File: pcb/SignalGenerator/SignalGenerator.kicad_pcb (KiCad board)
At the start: 2 copper layers, 29 parts, among them J1 ul.f antenna connector, U1 16 MHz, U2 MIC5205-3.3YM5, U3 AD9837, U4 AD8045

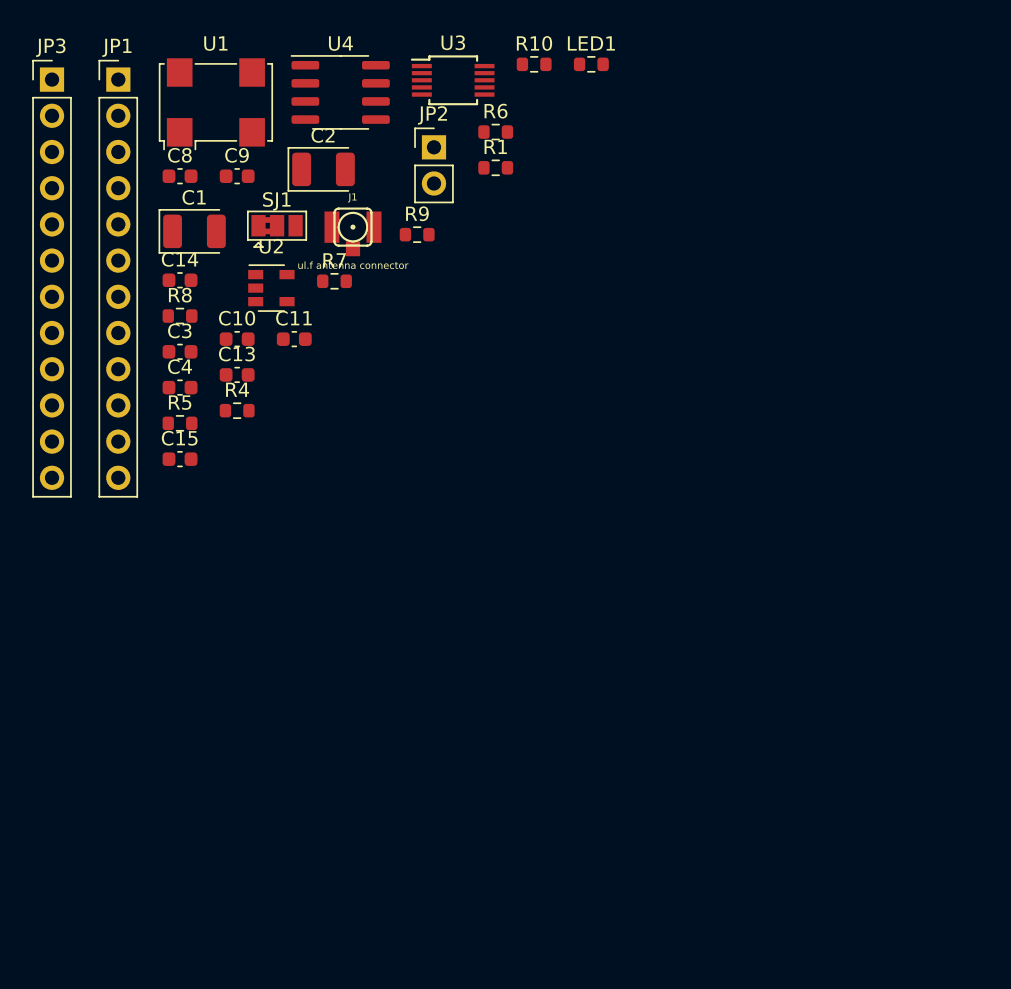
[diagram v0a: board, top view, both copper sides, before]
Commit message: Agrego modelo correcto para U3, y ubicación de los componentes
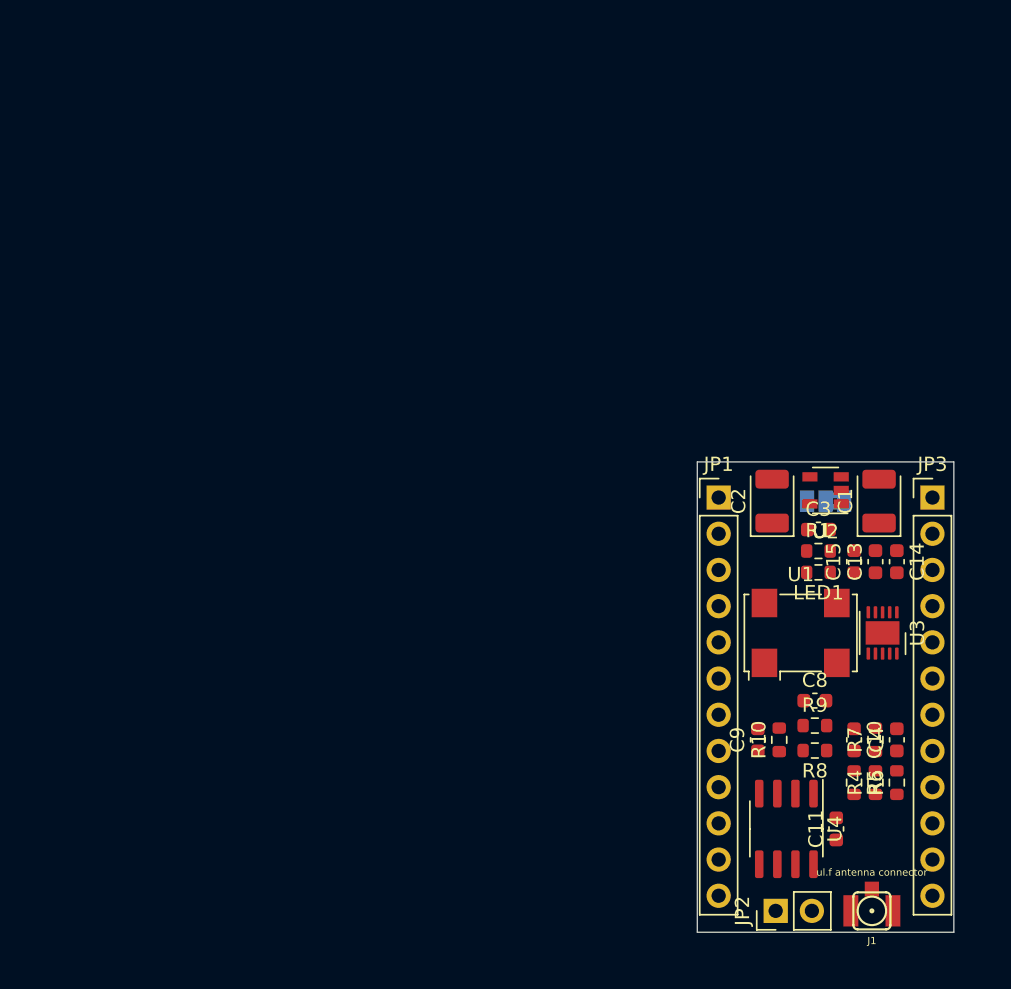
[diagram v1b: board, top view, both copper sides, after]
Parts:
- SJ1: moved to B.Cu
- U3: footprint Package_SO:MSOP-10_3x3mm_P0.5mm -> generador:LFCSP-WD-10-1EP_3x3mm_P0.5mm_EP1.64x2.38mm
- moved JP3 68.4 mm to (86.5, 52.5)
- moved U4 60.4 mm to (76.2, 75.8), turned to 270 degrees
- moved J1 60.2 mm to (82.2, 81.5), turned to 180 degrees
- moved JP2 58.7 mm to (75.5, 81.5), turned to 90 degrees
- moved C8 57.8 mm to (78.2, 66.8)
- moved C4 56.0 mm to (84.0, 69.5), turned to 90 degrees
- moved U1 55.4 mm to (77.2, 62.0)
- moved C14 54.0 mm to (84.0, 57.0), turned to 270 degrees
- moved R8 54.0 mm to (78.2, 70.2), turned to 180 degrees
- moved C9 53.8 mm to (74.2, 69.5), turned to 90 degrees
- moved R6 53.6 mm to (84.0, 72.5), turned to 90 degrees
- moved R5 53.6 mm to (81.0, 72.5), turned to 270 degrees
- moved R4 51.8 mm to (82.5, 72.5), turned to 90 degrees
- moved C1 51.6 mm to (82.8, 52.8), turned to 90 degrees
- moved C10 51.6 mm to (81.0, 69.5), turned to 270 degrees
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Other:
- board outline added: 18 x 33 mm

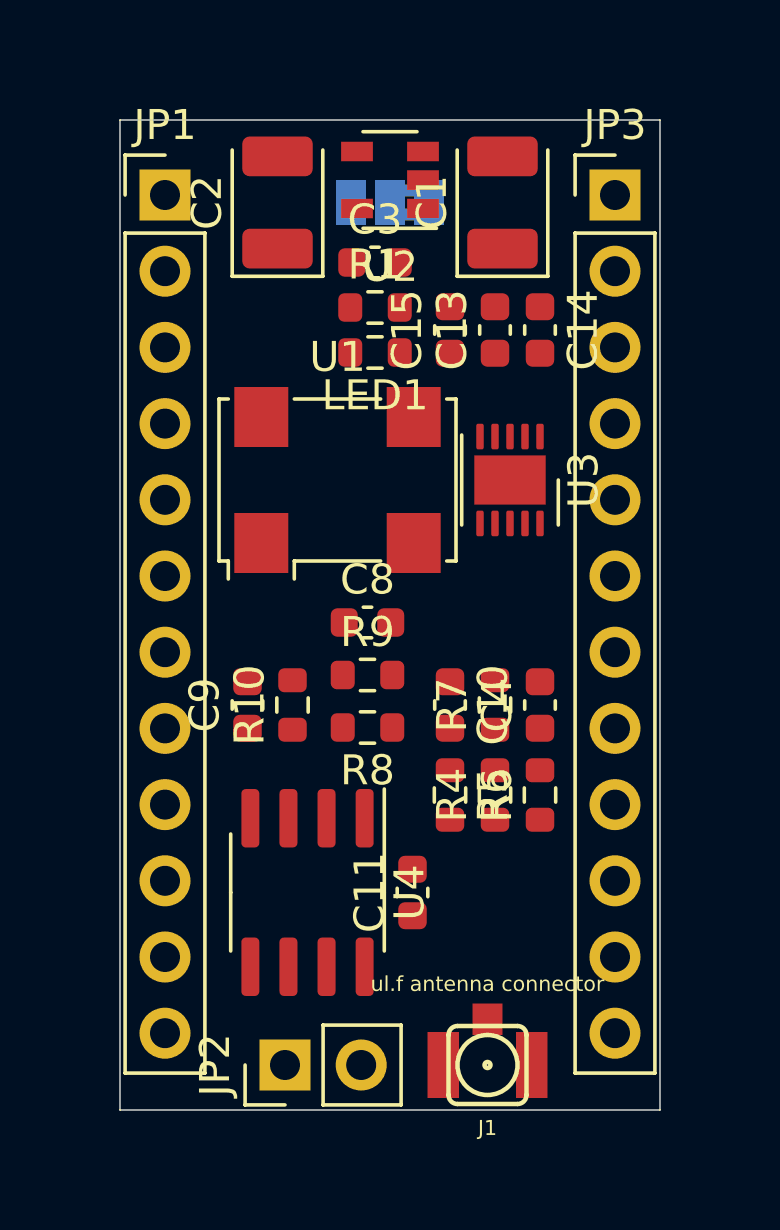
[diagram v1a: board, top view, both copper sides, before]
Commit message: Agrego routeo del PCB
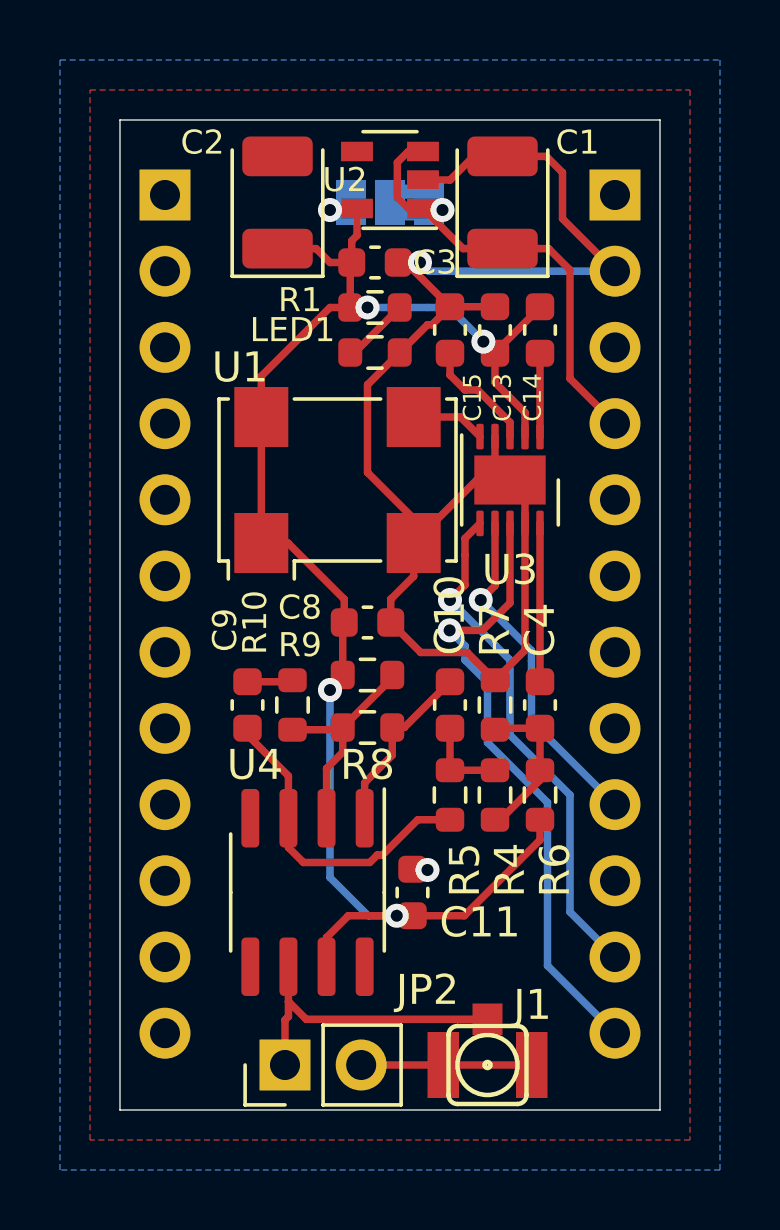
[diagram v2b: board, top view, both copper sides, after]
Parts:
- JP1, JP3: moved to B.Cu
- turned JP1 to 180 degrees
- turned JP3 to 180 degrees
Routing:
- net GND: track 0.00 -> 58.2 mm, vias 0 -> 2
- net VCC: track 0.00 -> 54.0 mm, vias 0 -> 5
- net /FSync: track 0.00 -> 20.8 mm, vias 0 -> 1
- net +BATT: track 0.00 -> 17.4 mm, vias 0 -> 1
- net /SData: track 0.00 -> 17.1 mm, vias 0 -> 1
- net /SCLK: track 0.00 -> 11.4 mm, vias 0 -> 1
- net Net-(C9-Pad1): track 0.00 -> 10.7 mm
- net /Output: track 0.00 -> 10.2 mm
- net Net-(R10-Pad1): track 0.00 -> 7.39 mm
- net Net-(C10-Pad1): track 0.00 -> 6.14 mm
- net Net-(C4-Pad1): track 0.00 -> 5.29 mm
- net /GeneratedSignal: track 0.00 -> 5.28 mm
- net Net-(C15-Pad1): track 0.00 -> 3.85 mm
- net Net-(C10-Pad2): track 0.00 -> 2.90 mm
- net Net-(C14-Pad2): track 0.00 -> 2.78 mm
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- added copper zone on B.Cu, net GND
- added copper zone on F.Cu, net GND
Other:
- board text added: "Grillas utilizadas: * 1 mm (contorno del PCB) * 0.25 mm (Componentes y pistas)"
- board text added: "Reglas de diseño: * 0,2 mm de clearence * 0,25 mm de separación de pistas * 0,8 mm pad de vía * 0,4 mm agujero de vía"
- board text added: "Stack de capas: * Top: F.cu * Bottom: B.cu"

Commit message: Cambios solicitados por el docente
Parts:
- added FID1: Fiducial, Fiducial:Fiducial_0.5mm_Mask1mm, F.Cu at (82.5, 78.2)
- added FID2: Fiducial, Fiducial:Fiducial_0.5mm_Mask1mm, F.Cu at (74.0, 56.1)
- LED1: footprint Resistor_SMD:R_0603_1608Metric -> LED_SMD:LED_0603_1608Metric
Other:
- board text added: "DCI - CESE Signal Generator Revisión 1.0"
- board text added: "Fabricante local contactado: * Ernesto Mayer"
- board text added: "Ind. Arg."
- board text added: "Terminación superficial: * HASL Lead free * Inmersion gold (segunda opción)"
